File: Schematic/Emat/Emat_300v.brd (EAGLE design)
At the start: 100 x 76.2 mm, 64 parts, among them IC1 UC3843N, J1 PIN1-2, J2 PIN1-2, J3 PIN1-2, J4 PIN1-2, J5 PIN1-2, J6 PIN1-2, Q1 BSS138, Q2 IRF640IW220B, T1 EFD25-2

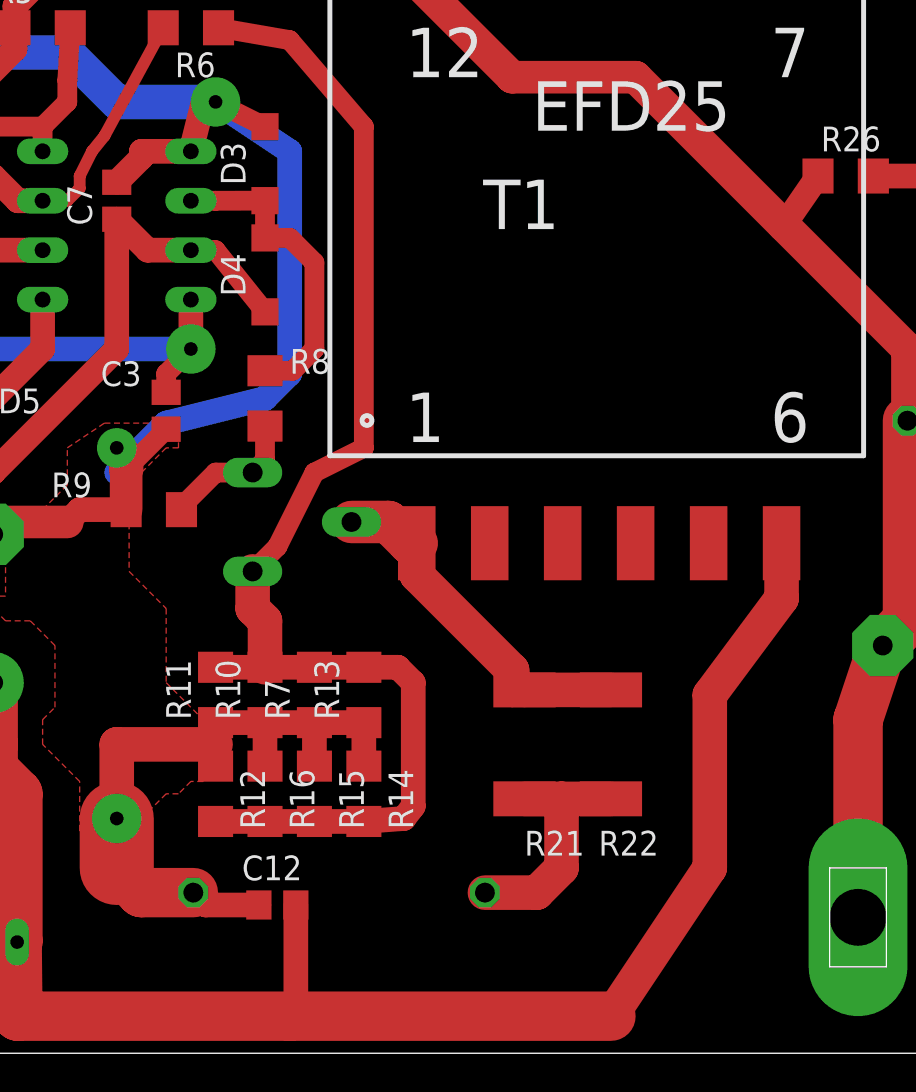
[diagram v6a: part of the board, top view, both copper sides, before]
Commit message: Fix transformer wiring.
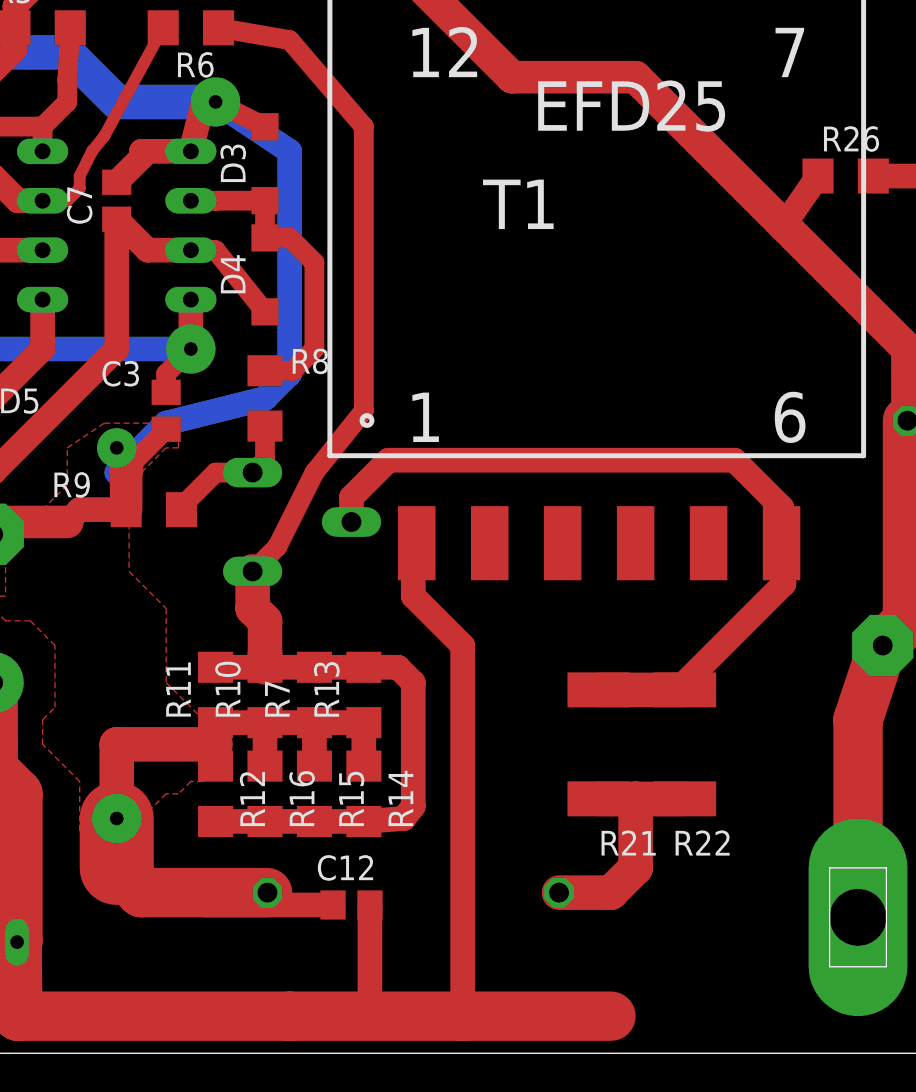
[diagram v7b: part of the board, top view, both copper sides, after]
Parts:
- moved C12 3.81 mm to (47.6, 7.62)
- moved R21 3.81 mm to (60.3, 15.9)
- moved C14 3.81 mm to (50.8, 8.26)
- moved R22 3.81 mm to (64.8, 15.9)
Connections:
- net +12V: now also T1.1; no longer T1.6
- net N$20: now also T1.6; no longer T1.1
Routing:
- net N$20: track 18.5 -> 41.2 mm
- net GND: track 202.6 -> 212.5 mm
- net +12V: track 153.1 -> 155.1 mm
- net N$13: track 67.5 -> 66.8 mm
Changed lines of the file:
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@@
 <attribute name="VALUE" x="27.94" y="14.605" size="1.27" layer="27" rot="R180"/>
 </element>
-<element name="C12" library="rcl" package="C0805" value="470nF" x="43.815" y="7.62" smashed="yes" rot="R180">
-<attribute name="NAME" x="45.085" y="10.16" size="1.27" layer="25" rot="R180"/>
-<attribute name="VALUE" x="46.355" y="6.35" size="1.27" layer="27" rot="R180"/>
+<element name="C12" library="rcl" package="C0805" value="470nF" x="47.625" y="7.62" smashed="yes" rot="R180">
+<attribute name="NAME" x="48.895" y="10.16" size="1.27" layer="25" rot="R180"/>
+<attribute name="VALUE" x="50.165" y="6.35" size="1.27" layer="27" rot="R180"/>
 </element>
 <element name="C13" library="rcl" package="C0805" value="470nF" x="21.59" y="9.525" smashed="yes" rot="R90">
@@
 <attribute name="VALUE" x="34.9758" y="66.675" size="1.27" layer="27" rot="R180"/>
 </element>
-<element name="R21" library="resistor" package="R2512" value="100" x="56.515" y="15.875" smashed="yes" rot="R90">
-<attribute name="NAME" x="56.515" y="10.16" size="1.27" layer="25"/>
-<attribute name="VALUE" x="55.245" y="20.32" size="1.27" layer="27"/>
-</element>
-<element name="R22" library="resistor" package="R2512" value="100" x="60.96" y="15.875" smashed="yes" rot="R90">
+<element name="R21" library="resistor" package="R2512" value="100" x="60.325" y="15.875" smashed="yes" rot="R90">
 <attribute name="NAME" x="60.325" y="10.16" size="1.27" layer="25"/>
-<attribute name="VALUE" x="60.325" y="20.955" size="1.27" layer="27"/>
-</element>
-<element name="C14" library="rcl" package="C150-064X183" value="1.2nF 630V K78-2" x="46.99" y="8.255" smashed="yes" rot="MR0">
-<attribute name="NAME" x="55.499" y="11.684" size="1.27" layer="26" ratio="10" rot="MR0"/>
-<attribute name="VALUE" x="52.959" y="2.413" size="1.27" layer="28" ratio="10" rot="MR0"/>
+<attribute name="VALUE" x="59.055" y="20.32" size="1.27" layer="27"/>
+</element>
+<element name="R22" library="resistor" package="R2512" value="100" x="64.77" y="15.875" smashed="yes" rot="R90">
+<attribute name="NAME" x="64.135" y="10.16" size="1.27" layer="25"/>
+<attribute name="VALUE" x="64.135" y="20.955" size="1.27" layer="27"/>
+</element>
+<element name="C14" library="rcl" package="C150-064X183" value="1.2nF 630V K78-2" x="50.8" y="8.255" smashed="yes" rot="MR0">
+<attribute name="NAME" x="63.119" y="11.684" size="1.27" layer="26" ratio="10" rot="MR0"/>
+<attribute name="VALUE" x="56.769" y="2.413" size="1.27" layer="28" ratio="10" rot="MR0"/>
 </element>
 <element name="D7" library="diode" package="DO201-15" value="MUR4100" x="72.39" y="66.04" smashed="yes" rot="MR180">
@@
 <wire x1="13.97" y1="36.195" x2="12.065" y2="34.29" width="2.54" layer="1"/>
 <via x="13.97" y="57.785" extent="1-16" drill="0.7" diameter="2.54"/>
-<wire x1="42.865" y1="7.62" x2="40.132" y2="7.62" width="1.27" layer="1"/>
-<wire x1="40.132" y1="7.62" x2="39.497" y2="8.255" width="1.27" layer="1"/>
+<wire x1="46.675" y1="7.62" x2="40.132" y2="7.62" width="1.27" layer="1"/>
+<wire x1="40.132" y1="7.62" x2="43.307" y2="8.255" width="1.27" layer="1"/>
 <wire x1="24.45" y1="15.875" x2="21.59" y2="15.875" width="1.27" layer="1"/>
 <wire x1="26.99" y1="47.625" x2="26.99" y2="50.165" width="1.27" layer="1"/>
@@
 <wire x1="16.83" y1="61.325" x2="14.24" y2="61.325" width="1.016" layer="1"/>
 <wire x1="14.24" y1="61.325" x2="13.97" y2="61.595" width="1.016" layer="1"/>
-<wire x1="39.497" y1="8.255" x2="36.83" y2="8.255" width="2.54" layer="1"/>
+<wire x1="43.307" y1="8.255" x2="36.83" y2="8.255" width="2.54" layer="1"/>
 <wire x1="36.83" y1="8.255" x2="35.56" y2="9.525" width="2.54" layer="1"/>
 <wire x1="40.64" y1="15.875" x2="35.56" y2="15.875" width="1.778" layer="1"/>
@@
 <wire x1="40.792" y1="52.705" x2="44.45" y2="52.07" width="1.016" layer="1"/>
 <wire x1="44.45" y1="52.07" x2="48.26" y2="47.625" width="1.016" layer="1"/>
-<wire x1="48.26" y1="47.625" x2="48.26" y2="31.115" width="1.016" layer="1"/>
+<wire x1="48.26" y1="47.625" x2="48.26" y2="33.02" width="1.016" layer="1"/>
 <wire x1="43.815" y1="26.035" x2="42.545" y2="24.765" width="1.016" layer="1"/>
 <wire x1="43.815" y1="26.035" x2="45.72" y2="29.845" width="1.016" layer="1"/>
-<wire x1="45.72" y1="29.845" x2="48.26" y2="31.115" width="1.016" layer="1"/>
+<wire x1="45.72" y1="29.845" x2="48.26" y2="33.02" width="1.016" layer="1"/>
 <wire x1="42.545" y1="24.765" x2="42.545" y2="22.86" width="1.778" layer="1"/>
 <wire x1="42.545" y1="22.86" x2="43.18" y2="22.225" width="1.778" layer="1"/>
@@
 <contactref element="C11" pad="1"/>
 <contactref element="C12" pad="1"/>
-<contactref element="T1" pad="6"/>
 <wire x1="30.48" y1="1.905" x2="44.45" y2="1.905" width="2.54" layer="1"/>
-<wire x1="44.45" y1="1.905" x2="60.96" y2="1.905" width="2.54" layer="1"/>
-<wire x1="60.96" y1="1.905" x2="66.04" y2="9.525" width="1.778" layer="1"/>
-<wire x1="69.73" y1="26.215" x2="69.73" y2="23.375" width="1.778" layer="1"/>
-<wire x1="69.73" y1="23.375" x2="66.04" y2="18.415" width="1.778" layer="1"/>
-<wire x1="66.04" y1="18.415" x2="66.04" y2="9.525" width="1.778" layer="1"/>
+<wire x1="44.45" y1="1.905" x2="53.34" y2="1.905" width="2.54" layer="1"/>
+<wire x1="53.34" y1="1.905" x2="60.96" y2="1.905" width="2.54" layer="1"/>
 <wire x1="30.44" y1="5.715" x2="30.48" y2="1.905" width="2.54" layer="1"/>
 <wire x1="29.21" y1="19.05" x2="29.21" y2="18.415" width="2.54" layer="1"/>
@@
 <wire x1="30.48" y1="5.715" x2="30.48" y2="5.675" width="1.27" layer="1"/>
 <wire x1="30.48" y1="5.675" x2="30.44" y2="5.715" width="1.27" layer="1"/>
-<wire x1="44.765" y1="7.62" x2="44.765" y2="2.22" width="1.27" layer="1"/>
-<wire x1="44.765" y1="2.22" x2="44.45" y2="1.905" width="1.27" layer="1"/>
+<wire x1="48.575" y1="7.62" x2="48.575" y2="2.22" width="1.27" layer="1"/>
+<wire x1="48.575" y1="2.22" x2="44.45" y2="1.905" width="1.27" layer="1"/>
 <wire x1="26.35" y1="15.875" x2="29.21" y2="15.875" width="1.27" layer="1"/>
 <wire x1="6.985" y1="5.08" x2="6.985" y2="38.252" width="1.27" layer="1"/>
 <wire x1="6.985" y1="38.252" x2="8.738" y2="40.005" width="1.27" layer="1"/>
+<contactref element="T1" pad="1"/>
+<wire x1="50.98" y1="26.215" x2="50.8" y2="26.035" width="1.27" layer="1"/>
+<wire x1="50.8" y1="26.035" x2="50.8" y2="23.495" width="1.27" layer="1"/>
+<wire x1="50.8" y1="23.495" x2="53.34" y2="20.955" width="1.27" layer="1"/>
+<wire x1="53.34" y1="20.955" x2="53.34" y2="1.905" width="1.27" layer="1"/>
 </signal>
 <signal name="N$16">
@@
 <contactref element="R21" pad="2"/>
 <contactref element="R22" pad="2"/>
-<contactref element="T1" pad="1"/>
-<wire x1="56.515" y1="18.675" x2="55.88" y2="18.675" width="1.778" layer="1"/>
-<wire x1="56.515" y1="18.675" x2="60.96" y2="18.675" width="1.778" layer="1"/>
-<wire x1="50.98" y1="26.215" x2="50.98" y2="24.585" width="1.778" layer="1"/>
-<wire x1="50.98" y1="24.585" x2="55.88" y2="19.685" width="1.778" layer="1"/>
-<wire x1="55.88" y1="19.685" x2="55.88" y2="18.675" width="1.778" layer="1"/>
-<wire x1="47.625" y1="27.305" x2="49.53" y2="27.305" width="2.1844" layer="1"/>
-<wire x1="50.98" y1="26.215" x2="50.62" y2="26.215" width="2.1844" layer="1"/>
-<wire x1="50.62" y1="26.215" x2="49.53" y2="27.305" width="2.1844" layer="1"/>
+<wire x1="60.325" y1="18.675" x2="64.77" y2="18.675" width="1.778" layer="1"/>
+<contactref element="T1" pad="6"/>
+<wire x1="47.625" y1="27.305" x2="47.625" y2="28.575" width="1.27" layer="1"/>
+<wire x1="47.625" y1="28.575" x2="49.53" y2="30.48" width="1.27" layer="1"/>
+<wire x1="49.53" y1="30.48" x2="67.31" y2="30.48" width="1.27" layer="1"/>
+<wire x1="67.31" y1="30.48" x2="69.73" y2="28.06" width="1.27" layer="1"/>
+<wire x1="69.73" y1="28.06" x2="69.73" y2="26.215" width="1.27" layer="1"/>
+<wire x1="69.73" y1="26.215" x2="69.85" y2="26.095" width="1.27" layer="1"/>
+<wire x1="69.85" y1="26.095" x2="69.85" y2="24.13" width="1.27" layer="1"/>
+<wire x1="69.85" y1="24.13" x2="64.77" y2="19.05" width="1.27" layer="1"/>
+<wire x1="64.77" y1="19.05" x2="64.77" y2="18.675" width="1.27" layer="1"/>
 </signal>
 <signal name="N$21">
@@
 <contactref element="C14" pad="1"/>
 <contactref element="R22" pad="1"/>
-<wire x1="56.515" y1="13.075" x2="58.42" y2="13.075" width="1.778" layer="1"/>
-<wire x1="58.42" y1="13.075" x2="60.96" y2="13.075" width="1.778" layer="1"/>
-<wire x1="54.483" y1="8.255" x2="57.15" y2="8.255" width="1.778" layer="1"/>
-<wire x1="57.15" y1="8.255" x2="58.42" y2="9.525" width="1.778" layer="1"/>
-<wire x1="58.42" y1="9.525" x2="58.42" y2="13.075" width="1.778" layer="1"/>
+<wire x1="60.325" y1="13.075" x2="62.23" y2="13.075" width="1.778" layer="1"/>
+<wire x1="62.23" y1="13.075" x2="64.77" y2="13.075" width="1.778" layer="1"/>
+<wire x1="58.293" y1="8.255" x2="60.96" y2="8.255" width="1.778" layer="1"/>
+<wire x1="60.96" y1="8.255" x2="62.23" y2="9.525" width="1.778" layer="1"/>
+<wire x1="62.23" y1="9.525" x2="62.23" y2="13.075" width="1.778" layer="1"/>
 </signal>
 <signal name="N$22">

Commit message: Fix schematic. 1.5KE300 added.
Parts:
- D2: value 1.5KE15A -> 1.5KE300A
- R27: value 510 -> 100
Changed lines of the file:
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@@
 <attribute name="VALUE" x="59.69" y="71.374" size="1.27" layer="27" ratio="10" rot="R180"/>
 </element>
-<element name="D2" library="diode" package="DO201-15" value="1.5KE15A" x="57.15" y="62.23" smashed="yes" rot="R180">
+<element name="D2" library="diode" package="DO201-15" value="1.5KE300A" x="57.15" y="62.23" smashed="yes" rot="R180">
 <attribute name="NAME" x="62.23" y="59.055" size="1.27" layer="25" ratio="10" rot="R180"/>
 <attribute name="VALUE" x="59.69" y="64.389" size="1.27" layer="27" ratio="10" rot="R180"/>
@@
 <attribute name="VALUE" x="66.04" y="44.45" size="1.27" layer="27"/>
 </element>
-<element name="R27" library="resistor" package="R1206" value="510" x="22.86" y="71.755" smashed="yes" rot="R180">
+<element name="R27" library="resistor" package="R1206" value="100" x="22.86" y="71.755" smashed="yes" rot="R180">
 <attribute name="NAME" x="21.59" y="74.295" size="1.27" layer="25" rot="R180"/>
 <attribute name="VALUE" x="24.13" y="74.295" size="1.27" layer="27" rot="R180"/>
